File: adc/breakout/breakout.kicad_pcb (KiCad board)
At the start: 2 copper layers, 34.4 x 27.5 mm, 69 parts, among them J1 Conn_01x05_Pin, J2 Conn_01x05_Pin, J3 Conn_01x03_Pin, J4 Conn_01x06_Pin, U1 ESD5344D-TP, U2 ADS1261IRHBR, U3 ESD5344D-TP, U4 ESD5344D-TP, U5 TPS7A2050PDBVR, U6 TPS61252DSG, U7 XC6206P332MR

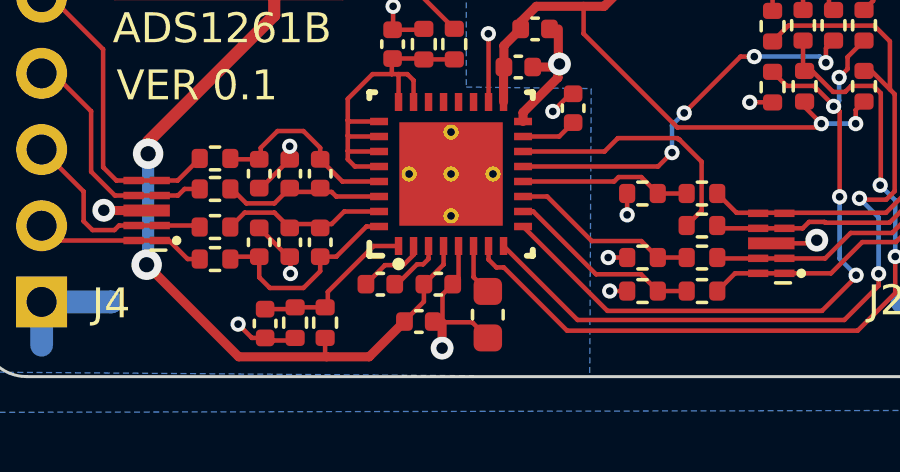
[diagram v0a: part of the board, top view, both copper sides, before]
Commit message: Fixed LCSC part number of LED resistor.
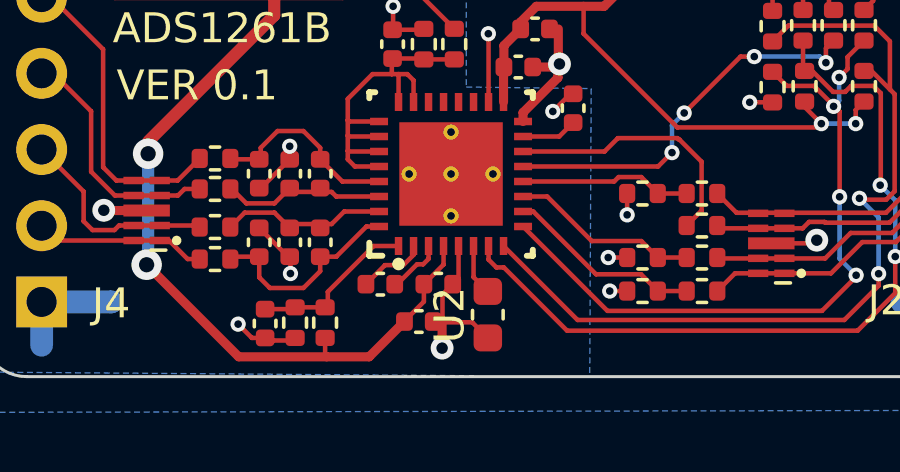
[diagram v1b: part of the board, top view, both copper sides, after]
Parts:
- R15: value 3K3 -> 5K1
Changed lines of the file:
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@@
   (net 44 "unconnected-(U6-PG-Pad5)")
   (net 45 "unconnected-(U5-NC-Pad4)")
-  (net 46 "Net-(J3-Pin_2)")
-  (net 47 "Net-(U5-EN)")
+  (net 46 "Net-(#FLG04-pwr)")
+  (net 47 "Net-(#FLG03-pwr)")
   (footprint "Resistor_SMD:R_0402_1005Metric" (layer "F.Cu")
     (at 28.3972 -11.7114 -90)
@@
       (stroke (width 0.1) (type solid)) (layer "F.Fab"))
     (pad "1" smd roundrect (at -1.4 0 270) (size 1.25 2.65) (layers "F.Cu" "F.Paste" "F.Mask") (roundrect_rratio 0.2)
-      (net 46 "Net-(J3-Pin_2)") (pinfunction "1") (pintype "passive"))
+      (net 46 "Net-(#FLG04-pwr)") (pinfunction "1") (pintype "passive"))
     (pad "2" smd roundrect (at 1.4 0 270) (size 1.25 2.65) (layers "F.Cu" "F.Paste" "F.Mask") (roundrect_rratio 0.2)
       (net 42 "Net-(U6-SW)") (pinfunction "2") (pintype "passive"))
@@
       (net 1 "GNDA") (pintype "passive"))
     (pad "2" smd roundrect (at 0.775 0 180) (size 0.9 0.95) (layers "F.Cu" "F.Paste" "F.Mask") (roundrect_rratio 0.25)
-      (net 47 "Net-(U5-EN)") (pintype "passive"))
+      (net 47 "Net-(#FLG03-pwr)") (pintype "passive"))
     (model "${KICAD6_3DMODEL_DIR}/Capacitor_SMD.3dshapes/C_0603_1608Metric.wrl"
       (offset (xyz 0 0 0))
@@
       (net 44 "unconnected-(U6-PG-Pad5)") (pinfunction "PG") (pintype "open_collector+no_connect"))
     (pad "6" smd rect (at 0.95 0.25) (size 0.5 0.25) (layers "F.Cu" "F.Paste" "F.Mask")
-      (net 46 "Net-(J3-Pin_2)") (pinfunction "EN") (pintype "input"))
+      (net 46 "Net-(#FLG04-pwr)") (pinfunction "EN") (pintype "input"))
     (pad "7" smd rect (at 0.95 -0.25) (size 0.5 0.25) (layers "F.Cu" "F.Paste" "F.Mask")
       (net 42 "Net-(U6-SW)") (pinfunction "SW") (pintype "passive"))
     (pad "8" smd rect (at 0.95 -0.75) (size 0.5 0.25) (layers "F.Cu" "F.Paste" "F.Mask")
-      (net 46 "Net-(J3-Pin_2)") (pinfunction "VIN") (pintype "power_in"))
+      (net 46 "Net-(#FLG04-pwr)") (pinfunction "VIN") (pintype "power_in"))
     (pad "9" smd rect (at 0 0) (size 0.9 1.6) (layers "F.Cu" "F.Mask")
       (net 4 "GNDD") (pinfunction "GND") (pintype "passive"))
@@
       (net 4 "GNDD") (pintype "passive"))
     (pad "2" smd roundrect (at 0.48 0 90) (size 0.56 0.62) (layers "F.Cu" "F.Paste" "F.Mask") (roundrect_rratio 0.25)
-      (net 46 "Net-(J3-Pin_2)") (pintype "passive"))
+      (net 46 "Net-(#FLG04-pwr)") (pintype "passive"))
     (model "${KICAD6_3DMODEL_DIR}/Capacitor_SMD.3dshapes/C_0402_1005Metric.wrl"
       (offset (xyz 0 0 0))
@@
     (descr "Resistor SMD 0402 (1005 Metric), square (rectangular) end terminal, IPC_7351 nominal, (Body size source: IPC-SM-782 page 72, https://www.pcb-3d.com/wordpress/wp-content/uploads/ipc-sm-782a_amendment_1_and_2.pdf), generated with kicad-footprint-generator")
     (tags "resistor")
-    (property "LCSC" "C25882")
+    (property "LCSC" "C25905")
     (property "Sheetfile" "breakout.kicad_sch")
     (property "Sheetname" "")
@@
         (effects (font (size 1 1) (thickness 0.15)))
     )
-    (fp_text value "3K3" (at 0 1.17 90) (layer "F.Fab")
+    (fp_text value "5K1" (at 0 1.17 90) (layer "F.Fab")
         (effects (font (size 1 1) (thickness 0.15)))
     )
@@
       (net 4 "GNDD") (pinfunction "Pin_1") (pintype "passive"))
     (pad "2" thru_hole oval (at 0 2.54 90) (size 1.7 1.7) (drill 1) (layers "*.Cu" "*.Mask")
-      (net 46 "Net-(J3-Pin_2)") (pinfunction "Pin_2") (pintype "passive"))
+      (net 46 "Net-(#FLG04-pwr)") (pinfunction "Pin_2") (pintype "passive"))
     (model "${KICAD6_3DMODEL_DIR}/Connector_PinHeader_2.54mm.3dshapes/PinHeader_1x02_P2.54mm_Vertical.wrl"
       (offset (xyz 0 0 -1.6))
@@
       (net 4 "GNDD") (pintype "passive"))
     (pad "2" smd roundrect (at 0.48 0) (size 0.56 0.62) (layers "F.Cu" "F.Paste" "F.Mask") (roundrect_rratio 0.25)
-      (net 46 "Net-(J3-Pin_2)") (pintype "passive"))
+      (net 46 "Net-(#FLG04-pwr)") (pintype "passive"))
     (model "${KICAD6_3DMODEL_DIR}/Capacitor_SMD.3dshapes/C_0402_1005Metric.wrl"
       (offset (xyz 0 0 0))
@@
       (net 3 "+3V3") (pinfunction "VOUT") (pintype "power_out"))
     (pad "3" smd roundrect (at 1.1375 0 90) (size 1.325 0.6) (layers "F.Cu" "F.Paste" "F.Mask") (roundrect_rratio 0.25)
-      (net 46 "Net-(J3-Pin_2)") (pinfunction "VIN") (pintype "power_in"))
+      (net 46 "Net-(#FLG04-pwr)") (pinfunction "VIN") (pintype "power_in"))
     (model "${KICAD6_3DMODEL_DIR}/Package_TO_SOT_SMD.3dshapes/SOT-23-3.wrl"
       (offset (xyz 0 0 0))
@@
       (net 10 "Net-(U6-VOUT)") (pintype "passive"))
     (pad "2" smd roundrect (at 1.0625 0 270) (size 0.875 1.2) (layers "F.Cu" "F.Paste" "F.Mask") (roundrect_rratio 0.25)
-      (net 47 "Net-(U5-EN)") (pintype "passive"))
+      (net 47 "Net-(#FLG03-pwr)") (pintype "passive"))
     (model "${KICAD6_3DMODEL_DIR}/Inductor_SMD.3dshapes/L_0805_2012Metric.wrl"
       (offset (xyz 0 0 0))
@@
       (stroke (width 0.1) (type solid)) (layer "F.Fab"))
     (pad "1" smd roundrect (at -1.1375 -0.95 270) (size 1.325 0.6) (layers "F.Cu" "F.Paste" "F.Mask") (roundrect_rratio 0.25)
-      (net 47 "Net-(U5-EN)") (pinfunction "IN") (pintype "power_in"))
+      (net 47 "Net-(#FLG03-pwr)") (pinfunction "IN") (pintype "power_in"))
     (pad "2" smd roundrect (at -1.1375 0 270) (size 1.325 0.6) (layers "F.Cu" "F.Paste" "F.Mask") (roundrect_rratio 0.25)
       (net 1 "GNDA") (pinfunction "GND") (pintype "power_in"))
     (pad "3" smd roundrect (at -1.1375 0.95 270) (size 1.325 0.6) (layers "F.Cu" "F.Paste" "F.Mask") (roundrect_rratio 0.25)
-      (net 47 "Net-(U5-EN)") (pinfunction "EN") (pintype "input"))
+      (net 47 "Net-(#FLG03-pwr)") (pinfunction "EN") (pintype "input"))
     (pad "4" smd roundrect (at 1.1375 0.95 270) (size 1.325 0.6) (layers "F.Cu" "F.Paste" "F.Mask") (roundrect_rratio 0.25)
       (net 45 "unconnected-(U5-NC-Pad4)") (pinfunction "NC") (pintype "passive+no_connect"))
@@
       (net 4 "GNDD") (pintype "passive"))
     (pad "2" smd roundrect (at 0.775 0 90) (size 0.9 0.95) (layers "F.Cu" "F.Paste" "F.Mask") (roundrect_rratio 0.25)
-      (net 46 "Net-(J3-Pin_2)") (pintype "passive"))
+      (net 46 "Net-(#FLG04-pwr)") (pintype "passive"))
     (model "${KICAD6_3DMODEL_DIR}/Capacitor_SMD.3dshapes/C_0603_1608Metric.wrl"
       (offset (xyz 0 0 0))
@@
       (net 4 "GNDD") (pintype "passive"))
     (pad "2" smd roundrect (at 0.775 0) (size 0.9 0.95) (layers "F.Cu" "F.Paste" "F.Mask") (roundrect_rratio 0.25)
-      (net 46 "Net-(J3-Pin_2)") (pintype "passive"))
+      (net 46 "Net-(#FLG04-pwr)") (pintype "passive"))
     (model "${KICAD6_3DMODEL_DIR}/Capacitor_SMD.3dshapes/C_0603_1608Metric.wrl"
       (offset (xyz 0 0 0))
@@
     (property "ki_keywords" "ADS1261IRHBR")
     (attr smd)
-    (fp_text reference "U2" (at -4.7 -0.05 90 unlocked) (layer "F.SilkS") hide
+    (fp_text reference "U2" (at -4.7 -0.05 90 unlocked) (layer "F.SilkS")
         (effects (font (size 1 1) (thickness 0.15)))
     )

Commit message: Removed yet another reference id from the top silkscreen.
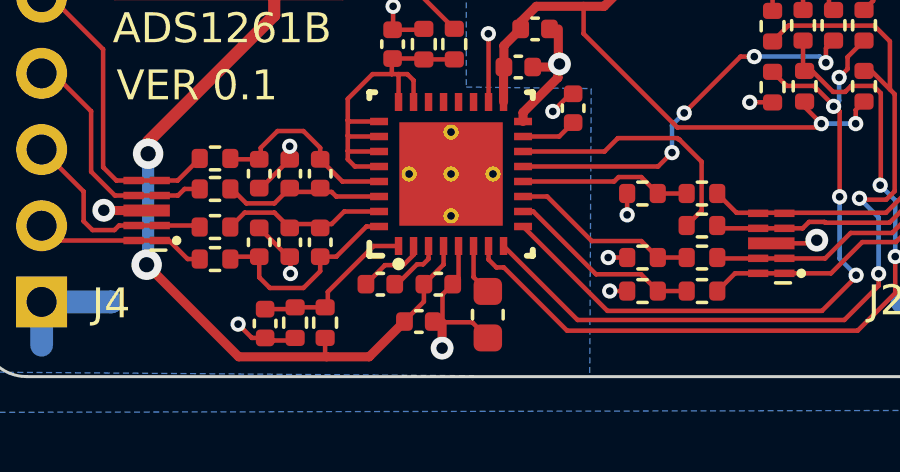
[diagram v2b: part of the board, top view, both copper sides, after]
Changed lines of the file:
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@@
   (net 44 "unconnected-(U6-PG-Pad5)")
   (net 45 "unconnected-(U5-NC-Pad4)")
-  (net 46 "Net-(#FLG04-pwr)")
-  (net 47 "Net-(#FLG03-pwr)")
+  (net 46 "Net-(J3-Pin_2)")
+  (net 47 "Net-(U5-EN)")
   (footprint "Resistor_SMD:R_0402_1005Metric" (layer "F.Cu")
     (at 28.3972 -11.7114 -90)
@@
       (stroke (width 0.1) (type solid)) (layer "F.Fab"))
     (pad "1" smd roundrect (at -1.4 0 270) (size 1.25 2.65) (layers "F.Cu" "F.Paste" "F.Mask") (roundrect_rratio 0.2)
-      (net 46 "Net-(#FLG04-pwr)") (pinfunction "1") (pintype "passive"))
+      (net 46 "Net-(J3-Pin_2)") (pinfunction "1") (pintype "passive"))
     (pad "2" smd roundrect (at 1.4 0 270) (size 1.25 2.65) (layers "F.Cu" "F.Paste" "F.Mask") (roundrect_rratio 0.2)
       (net 42 "Net-(U6-SW)") (pinfunction "2") (pintype "passive"))
@@
       (net 1 "GNDA") (pintype "passive"))
     (pad "2" smd roundrect (at 0.775 0 180) (size 0.9 0.95) (layers "F.Cu" "F.Paste" "F.Mask") (roundrect_rratio 0.25)
-      (net 47 "Net-(#FLG03-pwr)") (pintype "passive"))
+      (net 47 "Net-(U5-EN)") (pintype "passive"))
     (model "${KICAD6_3DMODEL_DIR}/Capacitor_SMD.3dshapes/C_0603_1608Metric.wrl"
       (offset (xyz 0 0 0))
@@
       (net 44 "unconnected-(U6-PG-Pad5)") (pinfunction "PG") (pintype "open_collector+no_connect"))
     (pad "6" smd rect (at 0.95 0.25) (size 0.5 0.25) (layers "F.Cu" "F.Paste" "F.Mask")
-      (net 46 "Net-(#FLG04-pwr)") (pinfunction "EN") (pintype "input"))
+      (net 46 "Net-(J3-Pin_2)") (pinfunction "EN") (pintype "input"))
     (pad "7" smd rect (at 0.95 -0.25) (size 0.5 0.25) (layers "F.Cu" "F.Paste" "F.Mask")
       (net 42 "Net-(U6-SW)") (pinfunction "SW") (pintype "passive"))
     (pad "8" smd rect (at 0.95 -0.75) (size 0.5 0.25) (layers "F.Cu" "F.Paste" "F.Mask")
-      (net 46 "Net-(#FLG04-pwr)") (pinfunction "VIN") (pintype "power_in"))
+      (net 46 "Net-(J3-Pin_2)") (pinfunction "VIN") (pintype "power_in"))
     (pad "9" smd rect (at 0 0) (size 0.9 1.6) (layers "F.Cu" "F.Mask")
       (net 4 "GNDD") (pinfunction "GND") (pintype "passive"))
@@
       (net 4 "GNDD") (pintype "passive"))
     (pad "2" smd roundrect (at 0.48 0 90) (size 0.56 0.62) (layers "F.Cu" "F.Paste" "F.Mask") (roundrect_rratio 0.25)
-      (net 46 "Net-(#FLG04-pwr)") (pintype "passive"))
+      (net 46 "Net-(J3-Pin_2)") (pintype "passive"))
     (model "${KICAD6_3DMODEL_DIR}/Capacitor_SMD.3dshapes/C_0402_1005Metric.wrl"
       (offset (xyz 0 0 0))
@@
       (net 4 "GNDD") (pinfunction "Pin_1") (pintype "passive"))
     (pad "2" thru_hole oval (at 0 2.54 90) (size 1.7 1.7) (drill 1) (layers "*.Cu" "*.Mask")
-      (net 46 "Net-(#FLG04-pwr)") (pinfunction "Pin_2") (pintype "passive"))
+      (net 46 "Net-(J3-Pin_2)") (pinfunction "Pin_2") (pintype "passive"))
     (model "${KICAD6_3DMODEL_DIR}/Connector_PinHeader_2.54mm.3dshapes/PinHeader_1x02_P2.54mm_Vertical.wrl"
       (offset (xyz 0 0 -1.6))
@@
       (net 4 "GNDD") (pintype "passive"))
     (pad "2" smd roundrect (at 0.48 0) (size 0.56 0.62) (layers "F.Cu" "F.Paste" "F.Mask") (roundrect_rratio 0.25)
-      (net 46 "Net-(#FLG04-pwr)") (pintype "passive"))
+      (net 46 "Net-(J3-Pin_2)") (pintype "passive"))
     (model "${KICAD6_3DMODEL_DIR}/Capacitor_SMD.3dshapes/C_0402_1005Metric.wrl"
       (offset (xyz 0 0 0))
@@
       (net 3 "+3V3") (pinfunction "VOUT") (pintype "power_out"))
     (pad "3" smd roundrect (at 1.1375 0 90) (size 1.325 0.6) (layers "F.Cu" "F.Paste" "F.Mask") (roundrect_rratio 0.25)
-      (net 46 "Net-(#FLG04-pwr)") (pinfunction "VIN") (pintype "power_in"))
+      (net 46 "Net-(J3-Pin_2)") (pinfunction "VIN") (pintype "power_in"))
     (model "${KICAD6_3DMODEL_DIR}/Package_TO_SOT_SMD.3dshapes/SOT-23-3.wrl"
       (offset (xyz 0 0 0))
@@
       (net 10 "Net-(U6-VOUT)") (pintype "passive"))
     (pad "2" smd roundrect (at 1.0625 0 270) (size 0.875 1.2) (layers "F.Cu" "F.Paste" "F.Mask") (roundrect_rratio 0.25)
-      (net 47 "Net-(#FLG03-pwr)") (pintype "passive"))
+      (net 47 "Net-(U5-EN)") (pintype "passive"))
     (model "${KICAD6_3DMODEL_DIR}/Inductor_SMD.3dshapes/L_0805_2012Metric.wrl"
       (offset (xyz 0 0 0))
@@
       (stroke (width 0.1) (type solid)) (layer "F.Fab"))
     (pad "1" smd roundrect (at -1.1375 -0.95 270) (size 1.325 0.6) (layers "F.Cu" "F.Paste" "F.Mask") (roundrect_rratio 0.25)
-      (net 47 "Net-(#FLG03-pwr)") (pinfunction "IN") (pintype "power_in"))
+      (net 47 "Net-(U5-EN)") (pinfunction "IN") (pintype "power_in"))
     (pad "2" smd roundrect (at -1.1375 0 270) (size 1.325 0.6) (layers "F.Cu" "F.Paste" "F.Mask") (roundrect_rratio 0.25)
       (net 1 "GNDA") (pinfunction "GND") (pintype "power_in"))
     (pad "3" smd roundrect (at -1.1375 0.95 270) (size 1.325 0.6) (layers "F.Cu" "F.Paste" "F.Mask") (roundrect_rratio 0.25)
-      (net 47 "Net-(#FLG03-pwr)") (pinfunction "EN") (pintype "input"))
+      (net 47 "Net-(U5-EN)") (pinfunction "EN") (pintype "input"))
     (pad "4" smd roundrect (at 1.1375 0.95 270) (size 1.325 0.6) (layers "F.Cu" "F.Paste" "F.Mask") (roundrect_rratio 0.25)
       (net 45 "unconnected-(U5-NC-Pad4)") (pinfunction "NC") (pintype "passive+no_connect"))
@@
       (net 4 "GNDD") (pintype "passive"))
     (pad "2" smd roundrect (at 0.775 0 90) (size 0.9 0.95) (layers "F.Cu" "F.Paste" "F.Mask") (roundrect_rratio 0.25)
-      (net 46 "Net-(#FLG04-pwr)") (pintype "passive"))
+      (net 46 "Net-(J3-Pin_2)") (pintype "passive"))
     (model "${KICAD6_3DMODEL_DIR}/Capacitor_SMD.3dshapes/C_0603_1608Metric.wrl"
       (offset (xyz 0 0 0))
@@
       (net 4 "GNDD") (pintype "passive"))
     (pad "2" smd roundrect (at 0.775 0) (size 0.9 0.95) (layers "F.Cu" "F.Paste" "F.Mask") (roundrect_rratio 0.25)
-      (net 46 "Net-(#FLG04-pwr)") (pintype "passive"))
+      (net 46 "Net-(J3-Pin_2)") (pintype "passive"))
     (model "${KICAD6_3DMODEL_DIR}/Capacitor_SMD.3dshapes/C_0603_1608Metric.wrl"
       (offset (xyz 0 0 0))
@@
     (property "ki_keywords" "ADS1261IRHBR")
     (attr smd)
-    (fp_text reference "U2" (at -4.7 -0.05 90 unlocked) (layer "F.SilkS")
+    (fp_text reference "U2" (at -0.073997 -0.179 unlocked) (layer "F.SilkS") hide
         (effects (font (size 1 1) (thickness 0.15)))
     )

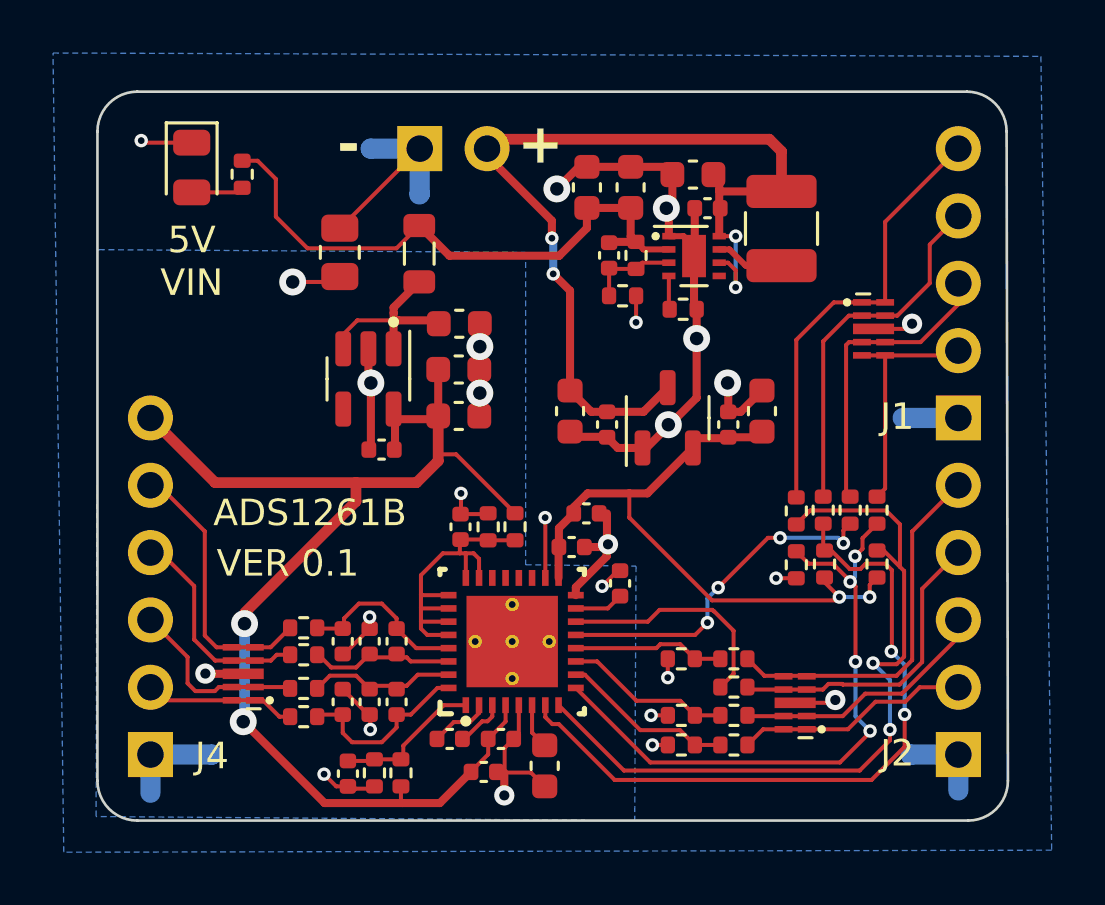
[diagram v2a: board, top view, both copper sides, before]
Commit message: Changed dc/dc/ voltage divider to JLCPCB Basic resistor values.
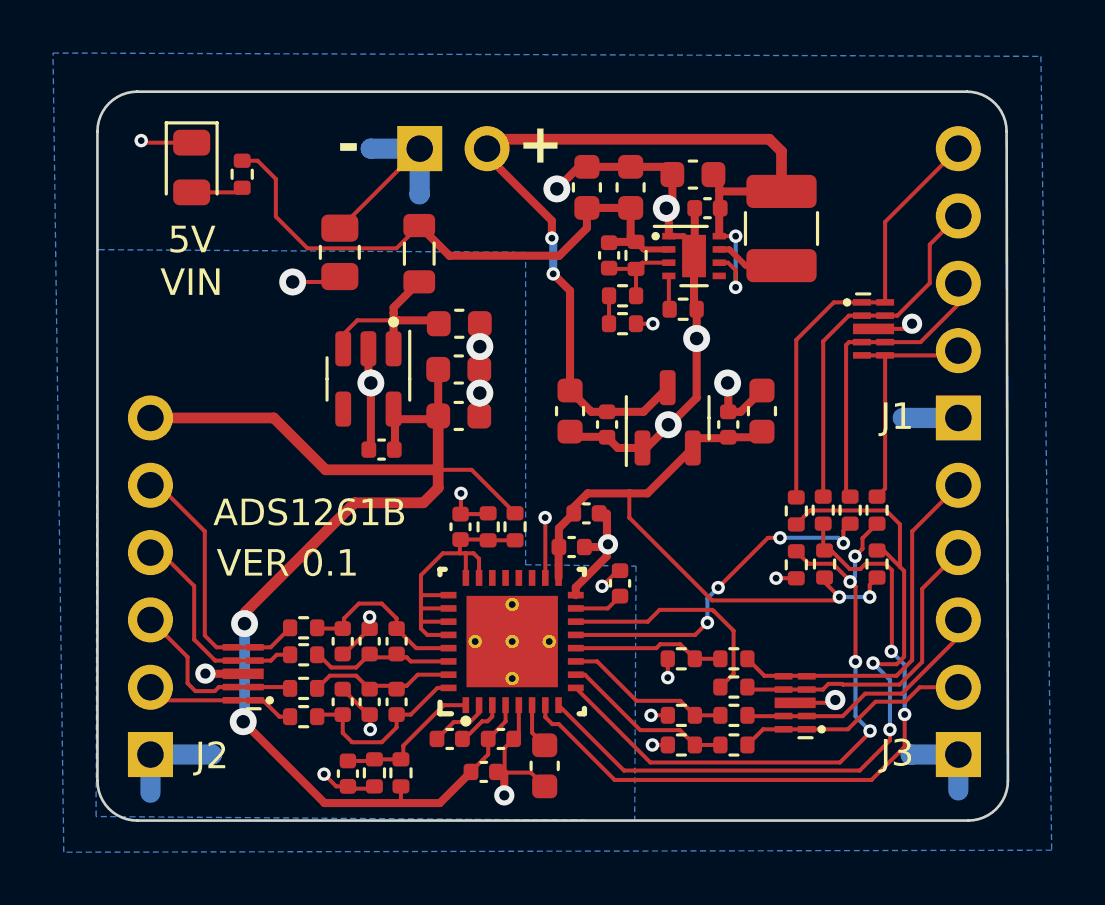
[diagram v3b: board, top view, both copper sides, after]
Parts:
- added R28: 22K, Resistor_SMD:R_0402_1005Metric, F.Cu at (19.8, -18.7)
- R23: renamed from R11; value 536K -> 510K
- R25: renamed from R13; value 150K -> 120K
- renumbered C12 to C10, C13 to C11, C6 to C12, C14 to C13, C7 to C14, C8 to C15, C18 to C16, C16 to C17, C20 to C18, C28 to C19, C19 to C20, C17 to C21, C21 to C24, C27 to C25, C24 to C27, C25 to C28, C15 to C5, C9 to C6, C10 to C7, C11 to C8, C5 to C9, FB5 to FB1, J4 to J2, J2 to J3, J3 to J4, R2 to R1, R28 to R10, R10 to R11, R8 to R12, R16 to R13, R29 to R14, R17 to R15, R18 to R16, R19 to R17, R20 to R18, R30 to R19, R6 to R2, R23 to R20, R24 to R21, R25 to R22, R15 to R24, R9 to R26, R21 to R27, R26 to R3, R1 to R4, R4 to R5, R5 to R6, R3 to R7, R14 to R8, R12 to R9, U4 to U2, U2 to U3, U3 to U4
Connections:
- R25 pad 1: Net-(U6-FB) -> Net-(R25-Pad1)
- R25 pad 2: GNDD -> Net-(U6-FB)
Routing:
- net +5VA: track 47.3 -> 50.2 mm
- net Net-(R25-Pad1): track 0.00 -> 1.05 mm

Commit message: Fixed the ADS1261 part value to ADS1261B.
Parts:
- U3: value ADS1261IRHBR -> ADS1261B
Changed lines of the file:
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@@
         (effects (font (size 1 1) (thickness 0.15)))
     )
-    (fp_text value "ADS1261IRHBR" (at -0.7 3.65 90 unlocked) (layer "F.Fab")
+    (fp_text value "ADS1261B" (at -0.7 3.65 90 unlocked) (layer "F.Fab")
         (effects (font (size 1 1) (thickness 0.15)))
     )

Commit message: Added net names to ADC breakout board schematic.
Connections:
- net Net-(J3-Pin_2) renamed /CS
- net Net-(J3-Pin_3) renamed /SCLK
- net Net-(J3-Pin_4) renamed /MISO
- net Net-(J3-Pin_5) renamed /MOSI
